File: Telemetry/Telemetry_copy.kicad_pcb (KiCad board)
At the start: 2 copper layers, 54 parts, among them J5 Conn_02x05_Odd_Even, Q3 Q_NMOS_GSD, SW1 SW_Push, SW3 SW_Push, U3 MAX485E, U4 STM32F103C8Tx, U5 LD1117S50TR_SOT223, U6 MCP1700-3302E_SOT23

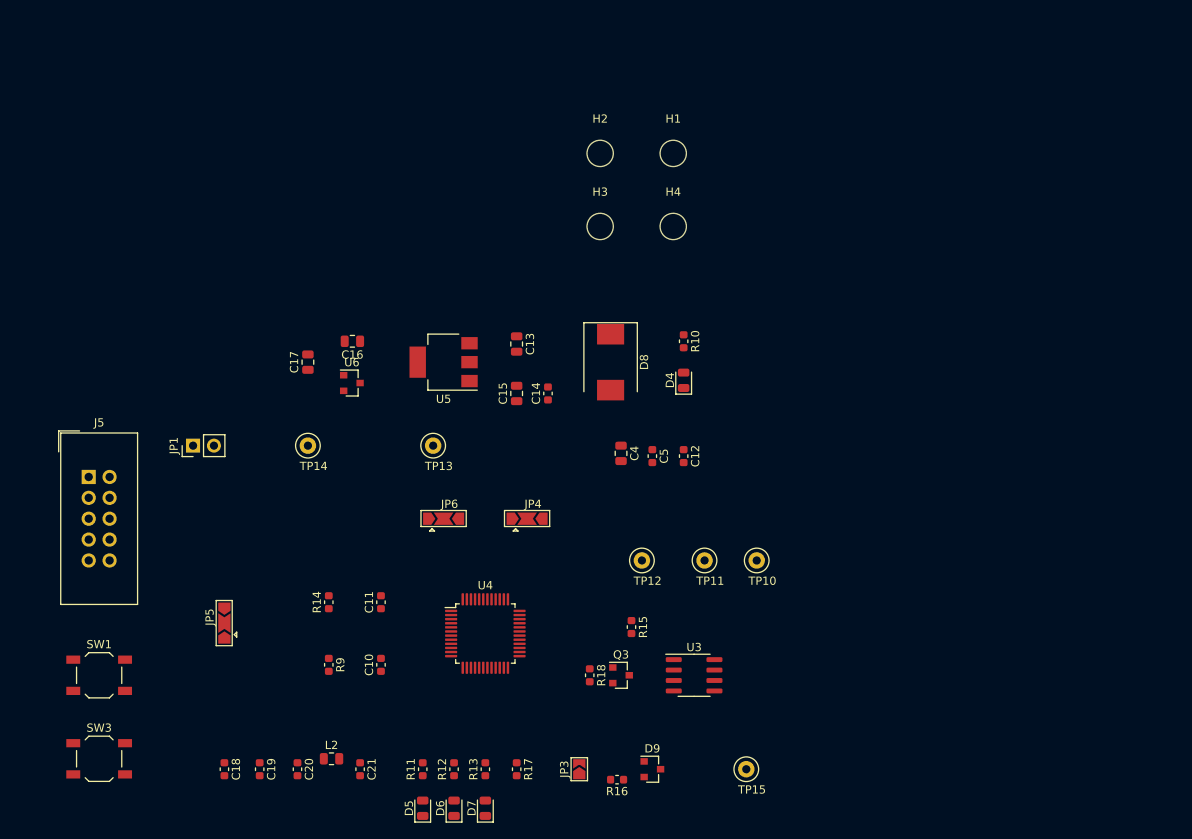
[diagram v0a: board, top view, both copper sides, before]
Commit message: Telemetry/: Update schema and create pcb layout
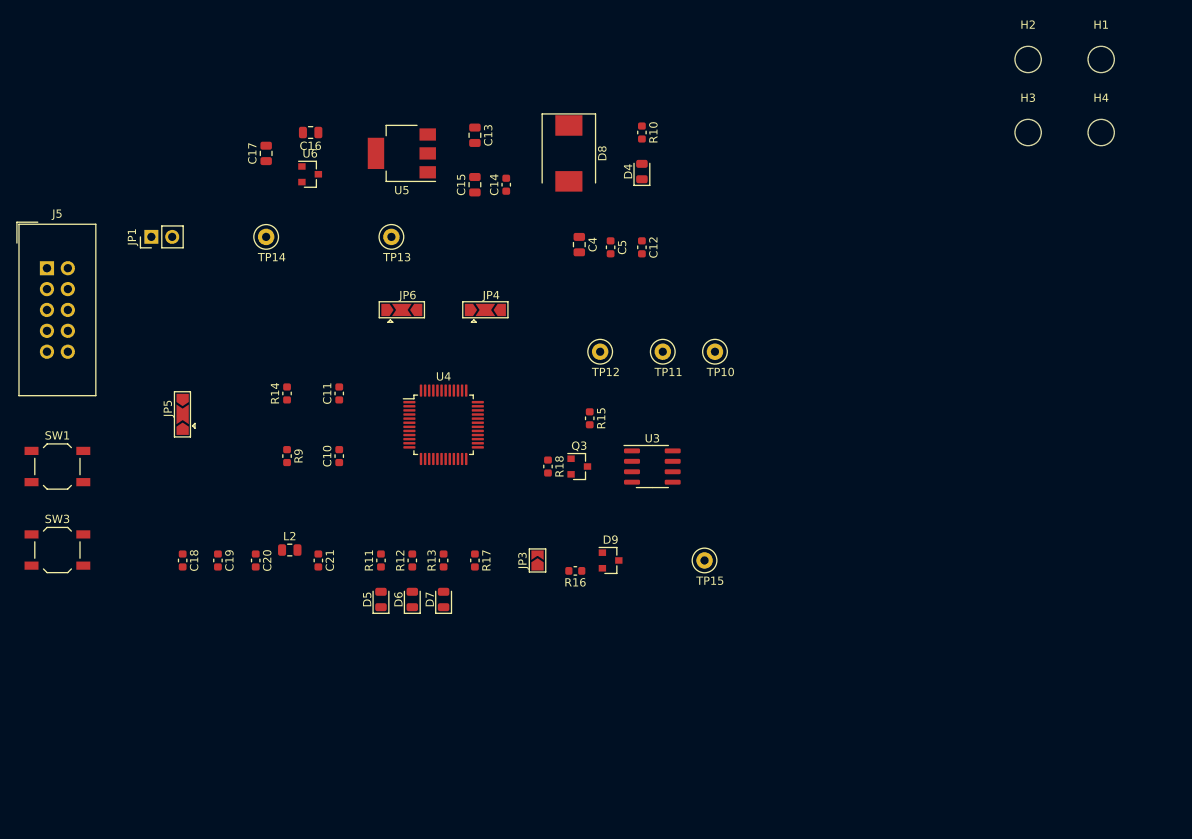
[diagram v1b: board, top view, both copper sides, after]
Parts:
- moved H2 53.3 mm to (146.1, 95.2)
- moved H3 53.3 mm to (146.1, 104.1)
- moved H1 53.3 mm to (154.9, 95.2)
- moved H4 53.3 mm to (154.9, 104.1)
- moved C10 25.9 mm to (62.2, 143.5)
- moved C11 25.9 mm to (62.2, 135.9)
- moved C13 25.9 mm to (78.7, 104.5)
- moved C17 25.9 mm to (53.3, 106.7)
- moved C18 25.9 mm to (43.2, 156.2)
- moved C19 25.9 mm to (47.5, 156.2)
- moved C20 25.9 mm to (52.1, 156.2)
- moved C21 25.9 mm to (59.7, 156.2)
- moved C4 25.9 mm to (91.4, 117.8)
- moved D8 25.9 mm to (90.2, 106.7)
- moved D9 25.9 mm to (95.2, 156.2)
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
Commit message: Telemetry/: Create a pcd layout
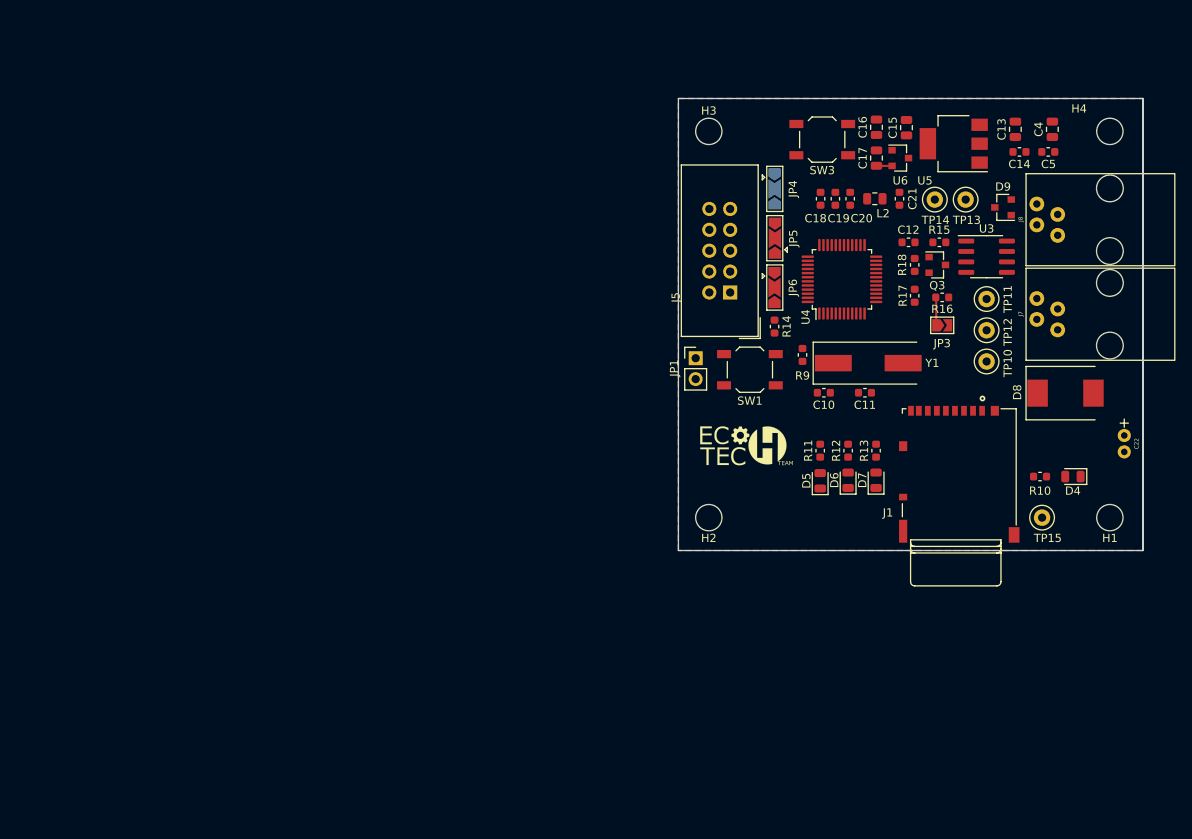
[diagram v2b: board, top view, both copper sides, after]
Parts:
- added C22: 100u, Footprints:C_Radial_D5.0mm_H11.0mm_P2.00mm, F.Cu at (157.8, 141.0)
- added G1: EchoTech Team, Footprints:EcoTech, F.Cu at (111.5, 142.5)
- added J1: Micro_SD_Card, Footprints:DM3AT-microSD, F.Cu at (137.2, 138.0)
- added J7: 4P4C, Footprints:4P4C, F.Cu at (156.0, 126.2)
- added J8: 4P4C, Footprints:4P4C, F.Cu at (156.0, 114.8)
- added Y1: 8Mhz, Footprints:Crystal_SMD_HC49-SD, F.Cu at (126.6, 132.2)
- moved SW3 105.6 mm to (121.0, 105.0), turned to 180 degrees
- moved C18 89.2 mm to (120.8, 112.2), turned to 90 degrees
- moved C19 87.1 mm to (122.6, 112.2), turned to 90 degrees
- moved SW1 85.1 mm to (112.2, 133.0), turned to 180 degrees
- moved C20 84.7 mm to (124.4, 112.2), turned to 90 degrees
- moved C21 83.3 mm to (130.4, 112.2), turned to 90 degrees
- moved J5 83.2 mm to (109.8, 123.6), turned to 180 degrees
- moved L2 83.0 mm to (127.4, 112.2)
- moved TP14 81.5 mm to (134.7, 112.3)
- moved JP5 75.2 mm to (115.2, 117.0)
- moved C17 74.3 mm to (127.6, 107.2)
- moved U6 71.8 mm to (130.5, 107.2)
- moved TP13 70.0 mm to (138.4, 112.3)
- moved C16 68.9 mm to (127.6, 103.5), turned to 90 degrees
- moved H2 68.0 mm to (107.2, 151.0)
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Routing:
- net Net-(JP3-Pad1): track 0.00 -> 3.47 mm
- net +3V3: track 0.00 -> 1.91 mm
- added copper zone on B.Cu, net GND
- added copper zone on F.Cu, net GND
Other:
- board outline added: 56.5 x 55 mm
- net class Default: trace_width 0.25 -> 0.2; via_dia 0.8 -> 0.7; via_drill 0.4 -> 0.3
- net class Signal added: clearance 0.2, trace_width 0.2, via_dia 0.7, via_drill 0.3
